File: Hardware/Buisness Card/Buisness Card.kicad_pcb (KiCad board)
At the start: 2 copper layers, 100.7 x 62.9 mm, 34 parts, among them J101 USB_A, J102 Conn_01x03_Male, J103 Tag Connect, P1 USB_A, U101 NCP1117-12_SOT223, U102 ATtiny85-20S, U103 ProtoBoard

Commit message: Change a few things maybe:
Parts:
- moved G*** 6.59 mm to (188.5, 119.6)
- moved REF** 6.59 mm to (190.0, 108.5)
- moved G*** 6.59 mm to (186.9, 114.2)
- moved G*** 0.25 mm to (195.8, 105.4)
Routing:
- net GND: track 0.00 -> 5.40 mm
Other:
- board text added: "${NAME}"
- board text added: "Find instructions on how to use with the QR code above!"
- board text added: "Kitsune Scientific ${EMAIL} ${DISCORD} ${WEBSITE} ${CALLSIGN}"
- board text removed: "${NAME} Kitsune Scientific ${EMAIL} ${DISCORD} ${WEBSITE} ${CALLSIGN}"
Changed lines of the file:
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@@
 (kicad_pcb (version 20211014) (generator pcbnew)
   (general
-    (thickness 1.6)
+    (thickness 1.2)
   )
   (paper "A4")
@@
       (layer "F.Mask" (type "Top Solder Mask") (thickness 0.01))
       (layer "F.Cu" (type "copper") (thickness 0.035))
-      (layer "dielectric 1" (type "core") (thickness 1.51) (material "FR4") (epsilon_r 4.5) (loss_tangent 0.02))
+      (layer "dielectric 1" (type "core") (thickness 1.11) (material "FR4") (epsilon_r 4.5) (loss_tangent 0.02))
       (layer "B.Cu" (type "copper") (thickness 0.035))
       (layer "B.Mask" (type "Bottom Solder Mask") (thickness 0.01))
@@
     )
   )
-  (property "CALLSIGN" "KW1FOX")
-  (property "DISCORD" "Snowsune#4646")
-  (property "EMAIL" "kenwood364@gmail.com")
-  (property "FULL_REVISION" "deletemelater")
+  (property "CALLSIGN" "Y0UR")
+  (property "DISCORD" "User#1000")
+  (property "EMAIL" "YourEmail@email.com")
+  (property "FULL_REVISION" "7f8f9bf")
   (property "ISSUE" "2022-08-10")
   (property "KENWOODFOX_3DMODELS" "Hardware/Buisness Card/Libraries/kenwoodfox-kicad-libraries/3d")
-  (property "NAME" "Joe Sedutto")
-  (property "REVISION" "c22958f")
-  (property "WEBSITE" "https://kitsunehosting.net/")
+  (property "NAME" "Your Name")
+  (property "REVISION" "7f8f9bf")
+  (property "WEBSITE" "https://YourWebsite.net/")
   (net 0 "")
   (net 1 "/SDO")
@@
   )
   (footprint "KenwoodFox:KITSUNE_LOGO" (layer "F.Cu")
-    (at 195.834 105.156)
+    (at 195.834 105.41)
     (attr board_only exclude_from_pos_files exclude_from_bom)
     (fp_text reference "G***" (at 0 0) (layer "F.SilkS")
@@
   )
   (footprint "Aesthetics:pcbway20x8" (layer "B.Cu")
-    (at 194.31 116.586 180)
+    (at 188.468 119.634 180)
     (attr through_hole)
     (fp_text reference "G***" (at 0 0) (layer "B.SilkS") hide
@@
     )
     (fp_line (start 6.03 0) (end 6.03 12) (layer "Dwgs.User") (width 0.15))
-    (fp_line (start 6.03 0) (end -6.03 0) (layer "Dwgs.User") (width 0.15))
     (fp_line (start -6.03 0) (end -6.03 12) (layer "Dwgs.User") (width 0.15))
+    (fp_line (start 6.03 0) (end -6.03 0) (layer "Dwgs.User") (width 0.15))
     (pad "1" connect rect locked (at 3.81 4.9 135) (size 1.9 8) (layers "B.Cu" "B.Mask"))
     (pad "2" connect rect locked (at 1.3 5.15 135) (size 2 7.5) (layers "B.Cu" "B.Mask"))
@@
   )
   (footprint "BuisnessCardSpecial:JLCPCB" (layer "B.Cu")
-    (at 192.785509 111.111322 180)
+    (at 186.943509 114.159322 180)
     (attr board_only exclude_from_pos_files exclude_from_bom)
     (fp_text reference "G***" (at 0 0) (layer "B.SilkS") hide
@@
   )
   (footprint "Symbol:KiCad-Logo2_5mm_SilkScreen" (layer "B.Cu")
-    (at 195.834 105.41 180)
+    (at 189.992 108.458 180)
     (descr "KiCad Logo")
     (tags "Logo KiCad")
@@
   (gr_arc (start 202.146 83.946) (mid 202.1528 80.4604) (end 205.6384 80.4672) (layer "Edge.Cuts") (width 0.1))
   (gr_line (start 114.3 123.19) (end 114.3 80.01) (layer "Edge.Cuts") (width 0.1))
-  (gr_text "JLCJLCJLCJLC" (at 118.364 101.6 -90) (layer "B.SilkS")
-    (effects (font (size 0.85 0.85) (thickness 0.2)) (justify mirror))
+  (gr_text "JLCJLCJLCJLC" (at 117.094 121.158 -90) (layer "B.SilkS")
+    (effects (font (size 0.85 0.85) (thickness 0.2)) (justify left mirror))
+  )
+  (gr_text "Find instructions on how to use\nwith the QR code above!" (at 197.866 101.092) (layer "B.SilkS")
+    (effects (font (size 0.7 0.7) (thickness 0.16)) (justify left mirror))
+  )
+  (gr_text "${NAME}" (at 202.692 112.014) (layer "F.SilkS")
+    (effects (font (size 2 2) (thickness 0.5)) (justify right))
   )
-  (gr_text "${NAME}\nKitsune Scientific\n\n${EMAIL}\n${DISCORD}\n${WEBSITE}\n${CALLSIGN}" (at 202.184 115.824) (layer "F.SilkS")
+  (gr_text "Kitsune Scientific\n${EMAIL}\n${DISCORD}\n${WEBSITE}\n${CALLSIGN}" (at 202.184 117.602) (layer "F.SilkS")
     (effects (font (size 1 1) (thickness 0.15)) (justify right))
   )
@@
   (segment (start 180.649826 81.788) (end 181.864 81.788) (width 0.4) (layer "F.Cu") (net 9))
   (segment (start 179.986913 82.450913) (end 180.649826 81.788) (width 0.4) (layer "F.Cu") (net 9))
+  (segment (start 197.9301 86.858054) (end 194.110154 90.678) (width 1.9) (layer "F.Cu") (net 10))
   (via (at 181.356 99.822) (size 0.8) (drill 0.4) (layers "F.Cu" "B.Cu") (free) (net 10))
   (via (at 117.856 86.36) (size 1.8) (drill 1.2) (layers "F.Cu" "B.Cu") (free) (net 10))
   (via (at 178.054 99.314) (size 0.8) (drill 0.4) (layers "F.Cu" "B.Cu") (free) (net 10))
-  (via (at 195.453 89.281) (size 0.8) (drill 0.4) (layers "F.Cu" "B.Cu") (net 10))
+  (via (at 191.2112 95.5548) (size 0.8) (drill 0.4) (layers "F.Cu" "B.Cu") (net 10))
   (segment (start 188.957953 93.880073) (end 189.853556 92.98447) (width 0.2) (layer "F.Cu") (net 12))
   (segment (start 186.436 94.742) (end 188.096026 94.742) (width 0.2) (layer "F.Cu") (net 12))

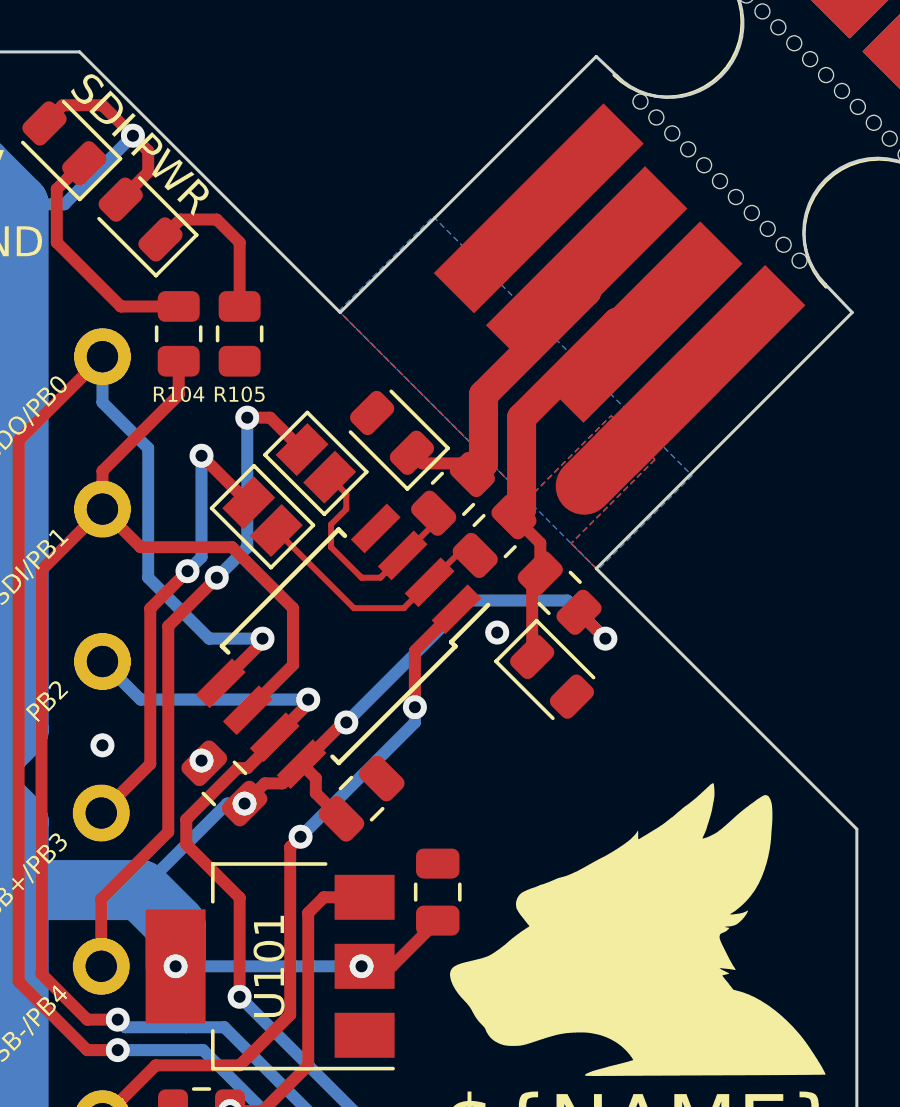
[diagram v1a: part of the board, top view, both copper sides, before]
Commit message: put diode in the right way
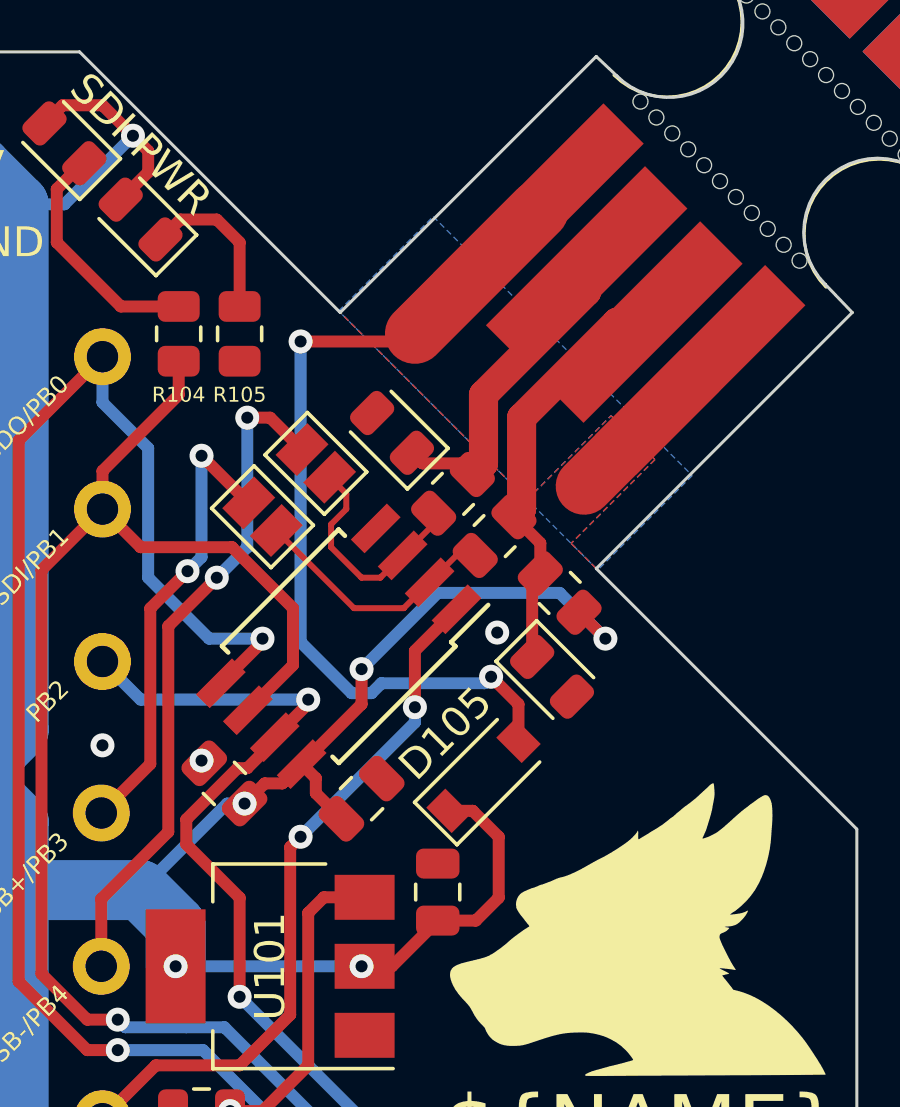
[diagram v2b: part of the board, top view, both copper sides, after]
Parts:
- added D105: MBR0520LT, Diode_SMD:D_SOD-123, F.Cu at (190.8, 100.3)
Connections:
- J101 pad 1: unconnected-(J101-Pad1) -> Net-(D105-Pad2)
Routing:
- net Net-(D105-Pad2): track 0.00 -> 29.6 mm, vias 0 -> 2
- net +5V: track 270.8 -> 278.1 mm
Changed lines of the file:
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@@
   (net 9 "Net-(D104-Pad1)")
   (net 10 "GND")
-  (net 11 "unconnected-(J101-Pad1)")
+  (net 11 "Net-(D105-Pad2)")
   (net 12 "/USB+")
   (net 13 "/USB-")
@@
     )
   )
+  (footprint "Diode_SMD:D_SOD-123" (layer "F.Cu")
+    (at 190.754 100.33 45)
+    (descr "SOD-123")
+    (tags "SOD-123")
+    (property "Sheetfile" "Buisness Card.kicad_sch")
+    (property "Sheetname" "")
+    (attr smd)
+    (fp_text reference "D105" (at 0.101975 -1.898026 45) (layer "F.SilkS")
+      (effects (font (size 1 1) (thickness 0.15)))
+    )
+    (fp_text value "MBR0520LT" (at -0.349999 0 45) (layer "F.Fab")
+      (effects (font (size 1 1) (thickness 0.15)))
+    )
+    (fp_text user "${REFERENCE}" (at 0 -2 45) (layer "F.Fab")
+      (effects (font (size 1 1) (thickness 0.15)))
+    )
+    (fp_line (start -2.25 1) (end 1.65 1) (layer "F.SilkS") (width 0.12))
+    (fp_line (start -2.25 -1) (end 1.65 -1) (layer "F.SilkS") (width 0.12))
+    (fp_line (start -2.25 -1) (end -2.25 1) (layer "F.SilkS") (width 0.12))
+    (fp_line (start 2.35 1.15) (end -2.35 1.15) (layer "F.CrtYd") (width 0.05))
+    (fp_line (start -2.35 -1.15) (end 2.35 -1.15) (layer "F.CrtYd") (width 0.05))
+    (fp_line (start -2.35 -1.15) (end -2.35 1.15) (layer "F.CrtYd") (width 0.05))
+    (fp_line (start 2.35 -1.15) (end 2.35 1.15) (layer "F.CrtYd") (width 0.05))
+    (fp_line (start -1.4 -0.9) (end 1.4 -0.9) (layer "F.Fab") (width 0.1))
+    (fp_line (start 1.4 0.9) (end -1.4 0.9) (layer "F.Fab") (width 0.1))
+    (fp_line (start -0.75 0) (end -0.35 0) (layer "F.Fab") (width 0.1))
+    (fp_line (start 1.4 -0.9) (end 1.4 0.9) (layer "F.Fab") (width 0.1))
+    (fp_line (start 0.25 0.4) (end -0.35 0) (layer "F.Fab") (width 0.1))
+    (fp_line (start 0.25 0) (end 0.75 0) (layer "F.Fab") (width 0.1))
+    (fp_line (start -0.35 0) (end 0.25 -0.4) (layer "F.Fab") (width 0.1))
+    (fp_line (start 0.25 -0.4) (end 0.25 0.4) (layer "F.Fab") (width 0.1))
+    (fp_line (start -0.35 0) (end -0.35 -0.55) (layer "F.Fab") (width 0.1))
+    (fp_line (start -1.4 0.9) (end -1.4 -0.9) (layer "F.Fab") (width 0.1))
+    (fp_line (start -0.35 0) (end -0.35 0.55) (layer "F.Fab") (width 0.1))
+    (pad "1" smd rect (at -1.65 0 45) (size 0.9 1.2) (layers "F.Cu" "F.Paste" "F.Mask")
+      (net 5 "+5V") (pinfunction "K") (pintype "passive"))
+    (pad "2" smd rect (at 1.65 0 45) (size 0.9 1.2) (layers "F.Cu" "F.Paste" "F.Mask")
+      (net 11 "Net-(D105-Pad2)") (pinfunction "A") (pintype "passive"))
+    (model "${KICAD6_3DMODEL_DIR}/Diode_SMD.3dshapes/D_SOD-123.wrl"
+      (offset (xyz 0 0 0))
+      (scale (xyz 1 1 1))
+      (rotate (xyz 0 0 0))
+    )
+  )
   (footprint "KenwoodFox:KITSUNE_LOGO" (layer "F.Cu")
     (at 195.834 105.41)
@@
     (fp_line (start 6.03 0) (end -6.03 0) (layer "Dwgs.User") (width 0.15))
     (pad "1" connect rect locked (at 3.81 -4.9 135) (size 1.9 8) (layers "F.Cu" "F.Paste" "F.Mask")
-      (net 11 "unconnected-(J101-Pad1)") (pinfunction "VBUS") (pintype "power_in"))
+      (net 11 "Net-(D105-Pad2)") (pinfunction "VBUS") (pintype "power_in"))
     (pad "2" connect rect locked (at 1.3 -5.15 135) (size 2 7.5) (layers "F.Cu" "F.Paste" "F.Mask")
       (net 6 "Net-(D101-Pad1)") (pinfunction "D-") (pintype "bidirectional"))
@@
   (segment (start 120.904 100.33) (end 171.704 100.33) (width 2) (layer "F.Cu") (net 5))
   (segment (start 183.461502 100.584) (end 184.050077 100.584) (width 0.4) (layer "F.Cu") (net 5))
-  (segment (start 186.182 98.552) (end 186.082077 98.552) (width 0.4) (layer "F.Cu") (net 5))
   (segment (start 190.5 122.7455) (end 190.5 123.571) (width 0.4) (layer "F.Cu") (net 5))
+  (segment (start 190.5 105.156) (end 189.23 105.156) (width 0.4) (layer "F.Cu") (net 5))
+  (segment (start 190.396726 101.496726) (end 191.262 102.362) (width 0.4) (layer "F.Cu") (net 5))
   (segment (start 185.166 100.911502) (end 186.018249 101.763751) (width 0.4) (layer "F.Cu") (net 5))
   (segment (start 179.07 78.994) (end 179.578 79.502) (width 0.4) (layer "F.Cu") (net 5))
+  (segment (start 191.262 102.362) (end 191.262 104.394) (width 0.4) (layer "F.Cu") (net 5))
   (segment (start 179.578 80.208174) (end 178.661087 81.125087) (width 0.4) (layer "F.Cu") (net 5))
   (segment (start 187.706 106.68) (end 186.792 106.68) (width 0.4) (layer "F.Cu") (net 5))
+  (segment (start 186.69 97.944077) (end 184.694099 99.939978) (width 0.4) (layer "F.Cu") (net 5))
   (segment (start 184.694099 99.939978) (end 185.166 100.411879) (width 0.4) (layer "F.Cu") (net 5))
-  (segment (start 186.082077 98.552) (end 184.694099 99.939978) (width 0.4) (layer "F.Cu") (net 5))
+  (segment (start 191.262 104.394) (end 190.5 105.156) (width 0.4) (layer "F.Cu") (net 5))
+  (segment (start 189.587274 101.496726) (end 190.396726 101.496726) (width 0.4) (layer "F.Cu") (net 5))
   (segment (start 175.26 119.888) (end 177.038 121.666) (width 0.4) (layer "F.Cu") (net 5))
   (segment (start 193.939235 94.879235) (end 194.818 95.758) (width 0.4) (layer "F.Cu") (net 5))
@@
   (segment (start 176.728174 77.978) (end 177.292 77.978) (width 0.4) (layer "F.Cu") (net 5))
   (segment (start 189.4205 121.666) (end 190.5 122.7455) (width 0.4) (layer "F.Cu") (net 5))
+  (segment (start 186.69 96.774) (end 186.69 97.944077) (width 0.4) (layer "F.Cu") (net 5))
   (segment (start 171.668627 120.65) (end 120.868627 120.65) (width 2) (layer "F.Cu") (net 5))
   (segment (start 175.26 119.38) (end 175.26 119.888) (width 0.4) (layer "F.Cu") (net 5))
@@
   (via (at 186.69 106.68) (size 0.8) (drill 0.4) (layers "F.Cu" "B.Cu") (net 5))
   (via (at 180.492 106.68) (size 0.8) (drill 0.4) (layers "F.Cu" "B.Cu") (net 5))
-  (via (at 186.182 98.552) (size 0.8) (drill 0.4) (layers "F.Cu" "B.Cu") (net 5))
+  (via (at 186.69 96.774) (size 0.8) (drill 0.4) (layers "F.Cu" "B.Cu") (net 5))
   (segment (start 175.26 101.854) (end 175.26 104.14) (width 2) (layer "B.Cu") (net 5))
   (segment (start 175.26 98.806) (end 175.26 81.28) (width 2) (layer "B.Cu") (net 5))
+  (segment (start 189.23 94.234) (end 193.294 94.234) (width 0.4) (layer "B.Cu") (net 5))
   (segment (start 176.784 81.28) (end 175.26 81.28) (width 0.4) (layer "B.Cu") (net 5))
   (segment (start 175.26 104.14) (end 175.26 119.38) (width 2) (layer "B.Cu") (net 5))
@@
   (segment (start 175.26 119.38) (end 173.99 120.65) (width 2) (layer "B.Cu") (net 5))
   (segment (start 180.492 105.308) (end 180.492 106.68) (width 2) (layer "B.Cu") (net 5))
+  (segment (start 193.294 94.234) (end 194.818 95.758) (width 0.4) (layer "B.Cu") (net 5))
   (segment (start 179.324 104.14) (end 180.492 105.308) (width 2) (layer "B.Cu") (net 5))
-  (segment (start 186.182 98.552) (end 190.246 94.488) (width 0.4) (layer "B.Cu") (net 5))
-  (segment (start 193.548 94.488) (end 194.818 95.758) (width 0.4) (layer "B.Cu") (net 5))
   (segment (start 186.69 106.68) (end 180.492 106.68) (width 0.4) (layer "B.Cu") (net 5))
   (segment (start 173.736 100.33) (end 175.26 98.806) (width 2) (layer "B.Cu") (net 5))
   (segment (start 173.99 120.65) (end 171.668627 120.65) (width 2) (layer "B.Cu") (net 5))
+  (segment (start 186.69 96.774) (end 189.23 94.234) (width 0.4) (layer "B.Cu") (net 5))
   (segment (start 171.704 100.33) (end 173.736 100.33) (width 2) (layer "B.Cu") (net 5))
   (segment (start 175.26 81.28) (end 173.99 80.01) (width 2) (layer "B.Cu") (net 5))
   (segment (start 179.07 78.994) (end 176.784 81.28) (width 0.4) (layer "B.Cu") (net 5))
   (segment (start 173.99 80.01) (end 171.704 80.01) (width 2) (layer "B.Cu") (net 5))
-  (segment (start 190.246 94.488) (end 193.548 94.488) (width 0.4) (layer "B.Cu") (net 5))
   (segment (start 182.208249 101.255751) (end 179.324 104.14) (width 0.4) (layer "B.Cu") (net 5))
   (segment (start 190.01247 89.916) (end 190.383235 90.286765) (width 0.4) (layer "F.Cu") (net 6))
@@
   (via (at 178.054 99.314) (size 0.8) (drill 0.4) (layers "F.Cu" "B.Cu") (free) (net 10))
   (via (at 191.2112 95.5548) (size 0.8) (drill 0.4) (layers "F.Cu" "B.Cu") (net 10))
+  (segment (start 191.920726 99.163274) (end 191.920726 97.940726) (width 0.4) (layer "F.Cu") (net 11))
+  (segment (start 191.920726 97.940726) (end 191.008 97.028) (width 0.4) (layer "F.Cu") (net 11))
+  (segment (start 192.5961 81.4699) (end 188.468 85.598) (width 2) (layer "F.Cu") (net 11))
+  (segment (start 188.214 85.852) (end 188.468 85.598) (width 0.4) (layer "F.Cu") (net 11))
+  (segment (start 184.658 85.852) (end 188.214 85.852) (width 0.4) (layer "F.Cu") (net 11))
+  (via (at 191.008 97.028) (size 0.8) (drill 0.4) (layers "F.Cu" "B.Cu") (net 11))
+  (via (at 184.658 85.852) (size 0.8) (drill 0.4) (layers "F.Cu" "B.Cu") (net 11))
+  (segment (start 187.351371 97.244) (end 187.021371 97.574) (width 0.4) (layer "B.Cu") (net 11))
+  (segment (start 187.021371 97.574) (end 186.358629 97.574) (width 0.4) (layer "B.Cu") (net 11))
+  (segment (start 186.358629 97.574) (end 184.658 95.873371) (width 0.4) (layer "B.Cu") (net 11))
+  (segment (start 190.792 97.244) (end 187.351371 97.244) (width 0.4) (layer "B.Cu") (net 11))
+  (segment (start 184.658 95.873371) (end 184.658 85.852) (width 0.4) (layer "B.Cu") (net 11))
+  (segment (start 191.008 97.028) (end 190.792 97.244) (width 0.4) (layer "B.Cu") (net 11))
   (segment (start 188.957953 93.880073) (end 189.853556 92.98447) (width 0.2) (layer "F.Cu") (net 12))
   (segment (start 186.436 94.742) (end 188.096026 94.742) (width 0.2) (layer "F.Cu") (net 12))
